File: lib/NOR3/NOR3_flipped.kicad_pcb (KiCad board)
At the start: 2 copper layers, 6 parts

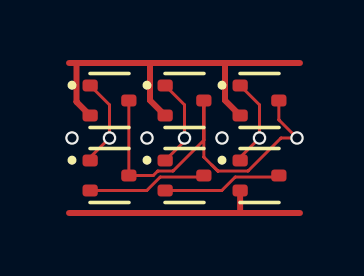
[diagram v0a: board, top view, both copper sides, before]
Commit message: High-density layout with pitch of 1.1mm, which gains 23% !!
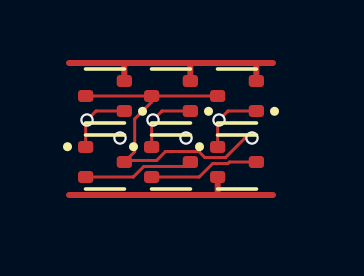
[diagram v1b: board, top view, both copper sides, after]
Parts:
- moved P3 0.87 mm to (5.50, 3.30)
- moved N3 0.76 mm to (5.50, 1.10), turned to 180 degrees
- moved P2 0.64 mm to (3.30, 3.30)
- moved N2 0.47 mm to (3.30, 1.10), turned to 180 degrees
- moved P1 0.47 mm to (1.10, 3.30)
- moved N1 0.21 mm to (1.10, 1.10), turned to 180 degrees
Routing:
- net GND: track 13.6 -> 8.61 mm
- net Y: track 14.0 -> 11.7 mm
- net VDD: track 8.45 -> 7.41 mm
- net C: track 3.03 -> 2.29 mm
- net B: track 3.03 -> 2.29 mm
- net A: track 3.03 -> 2.29 mm
- net (no net): vias 3 -> 2

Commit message: Same for NOR3
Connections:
- net A renamed A1
- net B renamed A2
- net C renamed A3
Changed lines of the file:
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@@
 	(net 1 "GND")
 	(net 2 "Y")
-	(net 3 "C")
+	(net 3 "A3")
 	(net 4 "VDD")
-	(net 5 "A")
-	(net 6 "B")
+	(net 5 "A1")
+	(net 6 "A2")
 	(net 7 "int1")
 	(net 8 "int2")
@@
 			(layers "F.Cu" "F.Mask" "F.Paste")
 			(roundrect_rratio 0.25)
-			(net 5 "A")
+			(net 5 "A1")
 			(pinfunction "G")
 			(pintype "inout")
@@
 			(layers "F.Cu" "F.Mask" "F.Paste")
 			(roundrect_rratio 0.25)
-			(net 3 "C")
+			(net 3 "A3")
 			(pinfunction "G")
 			(pintype "inout")
@@
 			(layers "F.Cu" "F.Mask" "F.Paste")
 			(roundrect_rratio 0.25)
-			(net 5 "A")
+			(net 5 "A1")
 			(pinfunction "G")
 			(pintype "inout")
@@
 			(layers "F.Cu" "F.Mask" "F.Paste")
 			(roundrect_rratio 0.25)
-			(net 6 "B")
+			(net 6 "A2")
 			(pinfunction "G")
 			(pintype "inout")
@@
 			(layers "F.Cu" "F.Mask" "F.Paste")
 			(roundrect_rratio 0.25)
-			(net 6 "B")
+			(net 6 "A2")
 			(pinfunction "G")
 			(pintype "inout")
@@
 			(layers "F.Cu" "F.Mask" "F.Paste")
 			(roundrect_rratio 0.25)
-			(net 3 "C")
+			(net 3 "A3")
 			(pinfunction "G")
 			(pintype "inout")

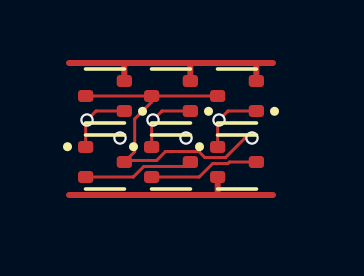
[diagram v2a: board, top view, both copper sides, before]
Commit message: All cells now use 1mm*4mm grid rather than 1.1mm*4.4mm
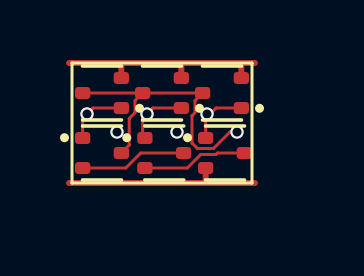
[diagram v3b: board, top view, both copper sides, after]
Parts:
- moved N3 0.51 mm to (5.00, 1.00)
- moved P3 0.50 mm to (5.10, 3.00)
- moved P2 0.37 mm to (3.08, 3.00)
- moved N2 0.32 mm to (3.00, 1.00)
- moved P1 0.32 mm to (1.00, 3.00)
- moved N1 0.14 mm to (1.00, 1.00)
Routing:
- net Y: track 11.7 -> 10.1 mm
- net GND: track 8.61 -> 7.77 mm
- net VDD: track 7.41 -> 6.62 mm

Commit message: Make the pads of my SOT523 footprint very slightly smaller, which is enough to route all the cells and leave the mosfets exactly on the grid
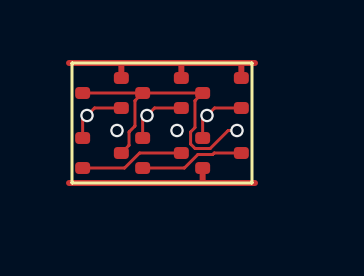
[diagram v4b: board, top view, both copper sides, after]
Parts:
- N1, N2, N3, P1, P2, P3: footprint Package_TO_SOT_SMD:SOT-523 -> RV523:SOT523
- moved P3 0.10 mm to (5.00, 3.00)
- moved P2 0.08 mm to (3.00, 3.00)

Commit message: Propagate MOSFET values to the cells' PCBs
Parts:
- N1, N2, N3: value (none) -> NMOS
- P1, P2, P3: value (none) -> PMOS
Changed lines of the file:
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@@
 			)
 		)
-		(property "Value" ""
+		(property "Value" "NMOS"
 			(at 0 0 180)
 			(layer "F.Fab")
@@
 			)
 		)
-		(property "Value" ""
+		(property "Value" "NMOS"
 			(at 0 0 180)
 			(layer "F.Fab")
@@
 			)
 		)
-		(property "Value" ""
+		(property "Value" "PMOS"
 			(at 0 0 0)
 			(layer "F.Fab")
@@
 			)
 		)
-		(property "Value" ""
+		(property "Value" "NMOS"
 			(at 0 0 180)
 			(layer "F.Fab")
@@
 			)
 		)
-		(property "Value" ""
+		(property "Value" "PMOS"
 			(at 0 0 0)
 			(layer "F.Fab")
@@
 			)
 		)
-		(property "Value" ""
-			(at 0 0 0)
-			(layer "F.Fab")
+		(property "Value" "PMOS"
+			(at 0 0 0)
+			(layer "F.Fab")
